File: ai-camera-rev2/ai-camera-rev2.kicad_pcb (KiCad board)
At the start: 4 copper layers, 70 x 70 mm, 178 parts, among them J1 Conn-01x02_P2mm_NONAME_JST-PH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, J2 TYPE-C-31-M-12, J3 MAXLAB, J4 Conn-02x10_P2.54mm_B-2100S20P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, J5 Conn-01x02_P1.25mm_10114829-1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, J6 Conn_01x24_FFC_0.5mm_AFC01-S2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, Q1 2N7002, Q10 2N7002, Q2 2N7002, Q3 AO3401A, Q4 AO3401A, Q5 2N7002, Q6 AO3401A, Q7 2N7002, Q8 AO3401A, Q9 2N7002, SW1 SW_PB_90deg_K2-1102AQ-H4CW-01, SW2 SW_PB_TS-1187A-B-A-B, SW3 SW_PB_TS-1187A-B-A-B, SW4 SW_PB_90deg_K2-1102AQ-H4CW-01, U1 TP4057-42-SOT26-R, U10 ESP32-S3-WROOM-1-N16R8, U11 MT9284-28J, U12 LTR-303ALS-01, U2 XC6206-2.8V, U3 PCF85063AT_SO8, U4 SOT-23-6_SN74LVC1G373DBVR_TI, U5 SY8089AAAC, U6 PIR_AS312, U7 XC6206-2.8V, U8 RT9166-12GVL, U9 AP1511B, Y1 32.768kHz_Q13FC1350000400

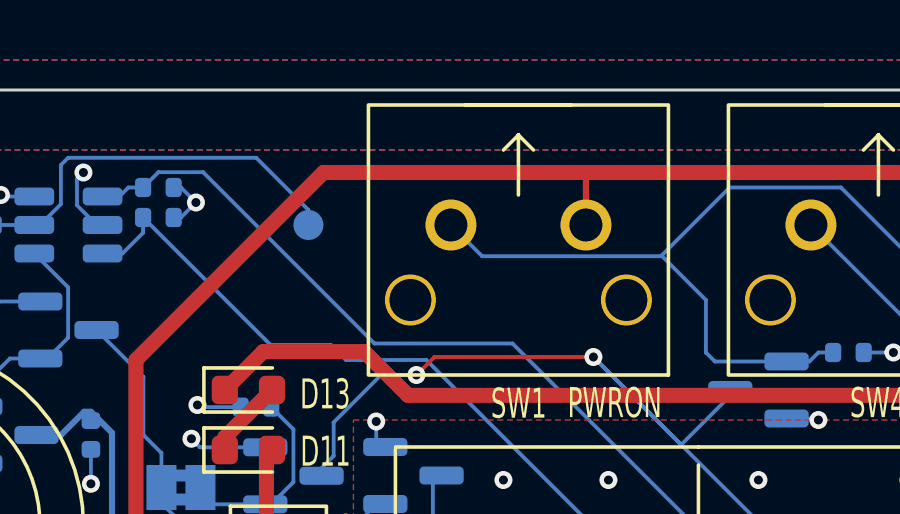
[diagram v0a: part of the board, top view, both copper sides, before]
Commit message: EAC-49: PWR_PIR instead of VBUS for PWRON button trigger
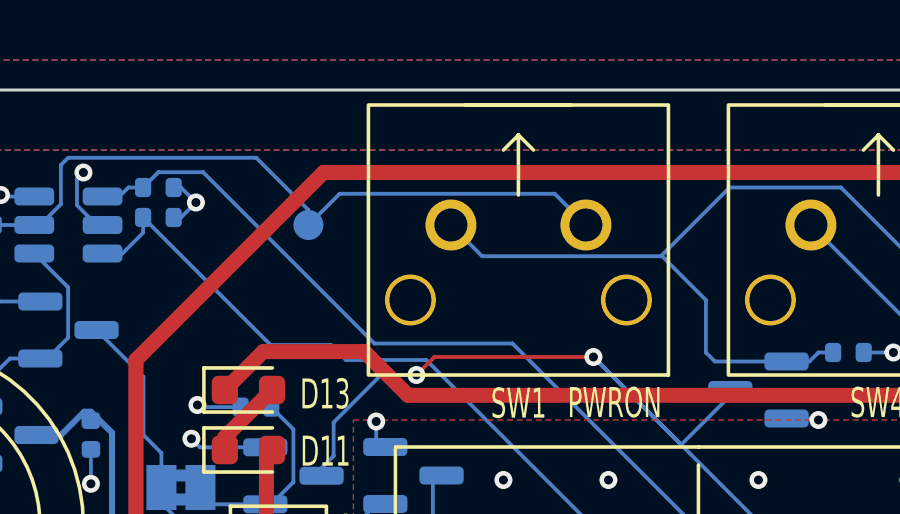
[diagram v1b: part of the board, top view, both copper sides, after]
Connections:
- SW1 pad 1: VBUS -> /PWR_PIR
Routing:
- net /PWR_PIR: track 48.6 -> 58.7 mm
- net VBUS: track 210.3 -> 208.5 mm
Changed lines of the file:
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@@
     (pad "" np_thru_hole circle locked (at 3.6 -2.5) (size 1.7 1.7) (drill 1.4) (layers "F&B.Cu" "*.Mask"))
     (pad "1" thru_hole circle locked (at -2.25 0) (size 1.7 1.7) (drill 1.1) (layers "*.Cu" "*.Mask")
-      (net 3 "VBUS") (pinfunction "1") (pintype "passive"))
+      (net 5 "/PWR_PIR") (pinfunction "1") (pintype "passive"))
     (pad "2" thru_hole circle locked (at 2.25 0) (size 1.7 1.7) (drill 1.1) (layers "*.Cu" "*.Mask")
       (net 59 "/PWRON_DET") (pinfunction "2") (pintype "passive"))
@@
   (segment (start 117.5 47.75) (end 111.25 54) (width 0.5) (layer "F.Cu") (net 3))
   (segment (start 99.85 74.49) (end 101.82 74.49) (width 0.5) (layer "F.Cu") (net 3))
-  (segment (start 126.25 47.9) (end 126.25 49.5) (width 0.2032) (layer "F.Cu") (net 3))
   (segment (start 137.88 106.78) (end 137.88 107.46) (width 0.2032) (layer "F.Cu") (net 3))
   (segment (start 124 100) (end 123.745 100) (width 0.2032) (layer "F.Cu") (net 3))
@@
   (segment (start 103.635 74.85) (end 103.91 74.575) (width 0.5) (layer "F.Cu") (net 3))
   (segment (start 136.72 106.62) (end 138.04 106.62) (width 0.2032) (layer "F.Cu") (net 3))
-  (segment (start 126.4 47.75) (end 126.25 47.9) (width 0.2032) (layer "F.Cu") (net 3))
   (segment (start 137.88 107.46) (end 138.415 107.995) (width 0.2032) (layer "F.Cu") (net 3))
   (segment (start 111.25 59.75) (end 107.25 63.75) (width 0.5) (layer "F.Cu") (net 3))
@@
   (segment (start 105.94 77.69) (end 106.771288 78.521288) (width 0.5) (layer "B.Cu") (net 4))
   (segment (start 101 57.48) (end 101.97 57.48) (width 0.127) (layer "B.Cu") (net 5))
+  (segment (start 125.2095 48.4595) (end 126.25 49.5) (width 0.127) (layer "B.Cu") (net 5))
   (segment (start 108.9905 47.2595) (end 115.2595 47.2595) (width 0.127) (layer "B.Cu") (net 5))
   (segment (start 106.5 49.5) (end 103.504 52.496) (width 0.127) (layer "B.Cu") (net 5))
@@
   (segment (start 102 57.51) (end 102.49 57.51) (width 0.127) (layer "B.Cu") (net 5))
   (segment (start 108.75 47.5) (end 108.9905 47.2595) (width 0.127) (layer "B.Cu") (net 5))
+  (segment (start 117 49.5) (end 118.0405 48.4595) (width 0.127) (layer "B.Cu") (net 5))
   (segment (start 117 49) (end 117 49.5) (width 0.127) (layer "B.Cu") (net 5))
   (segment (start 103.004 52.496) (end 98.75 56.75) (width 0.127) (layer "B.Cu") (net 5))
@@
   (segment (start 104.75 62.5) (end 104.75 59.77) (width 0.127) (layer "B.Cu") (net 5))
   (segment (start 102.49 57.51) (end 104.25 55.75) (width 0.127) (layer "B.Cu") (net 5))
+  (segment (start 118.0405 48.4595) (end 125.2095 48.4595) (width 0.127) (layer "B.Cu") (net 5))
   (segment (start 115.2595 47.2595) (end 117 49) (width 0.127) (layer "B.Cu") (net 5))
   (segment (start 103.504 52.496) (end 103.004 52.496) (width 0.127) (layer "B.Cu") (net 5))
